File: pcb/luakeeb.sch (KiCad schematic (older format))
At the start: 121 parts, among them J1 Pimoroni, J2 Conn_01x04_Female, J3 Conn_01x04_Female, SW1 SW_Push, SW10 SW_Push, SW11 SW_Push, SW12 SW_Push, SW13 SW_Push, SW14 SW_Push, SW15 SW_Push, SW16 SW_Push, SW2 SW_Push, SW21 SW_Push, SW22 SW_Push, SW23 SW_Push, SW24 SW_Push, SW25 SW_Push, SW3 SW_Push, SW34 SW_Push, SW35 SW_Push, SW4 SW_Push, SW41 SW_Push, SW42 RotaryEncoder_Switch, SW5 SW_Push, SW6 SW_Push, SW7 RotaryEncoder_Switch, SW8 SW_Push, SW9 SW_Push, U1 ProMicro, U3 TRRS, U4 TRRS

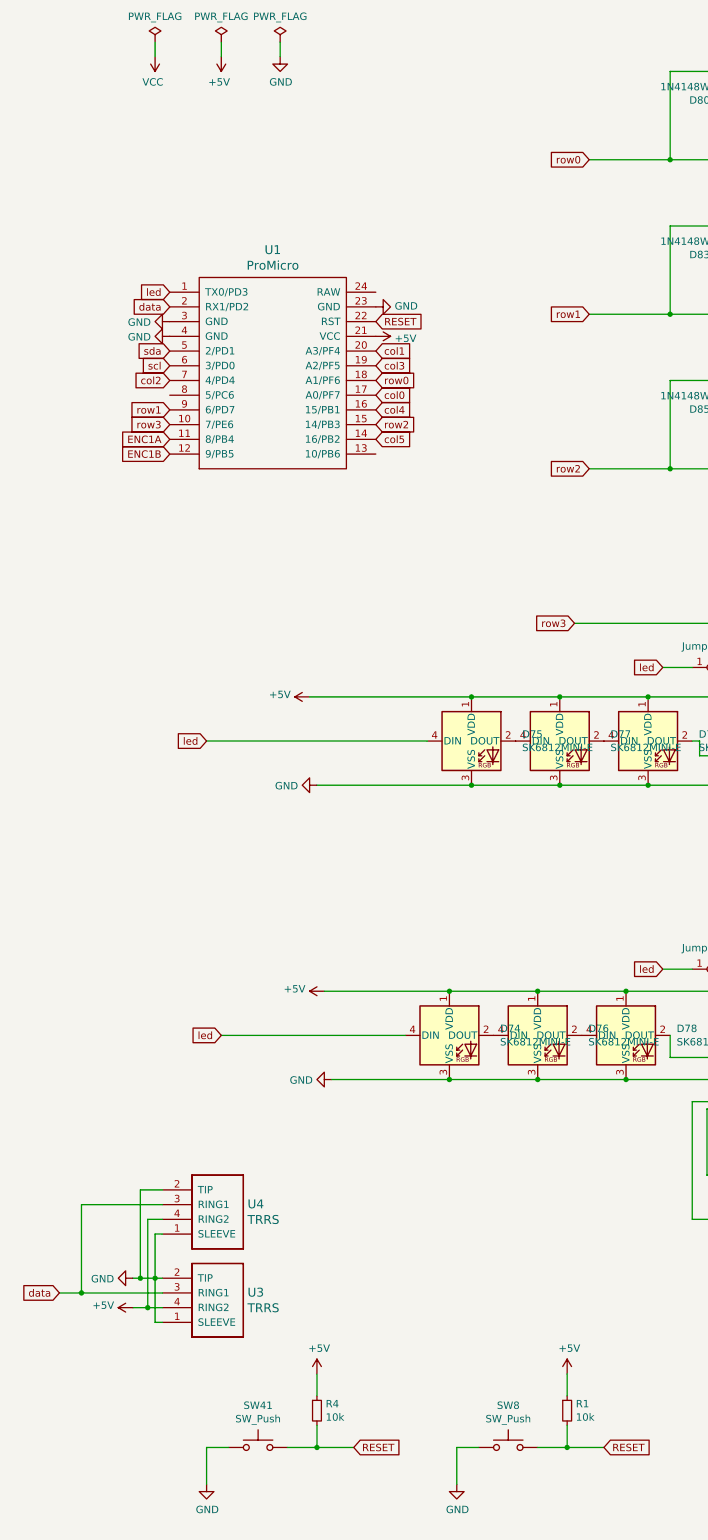
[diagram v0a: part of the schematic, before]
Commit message: added wireless support for nice nano with wiring, jst connector, and on off switch
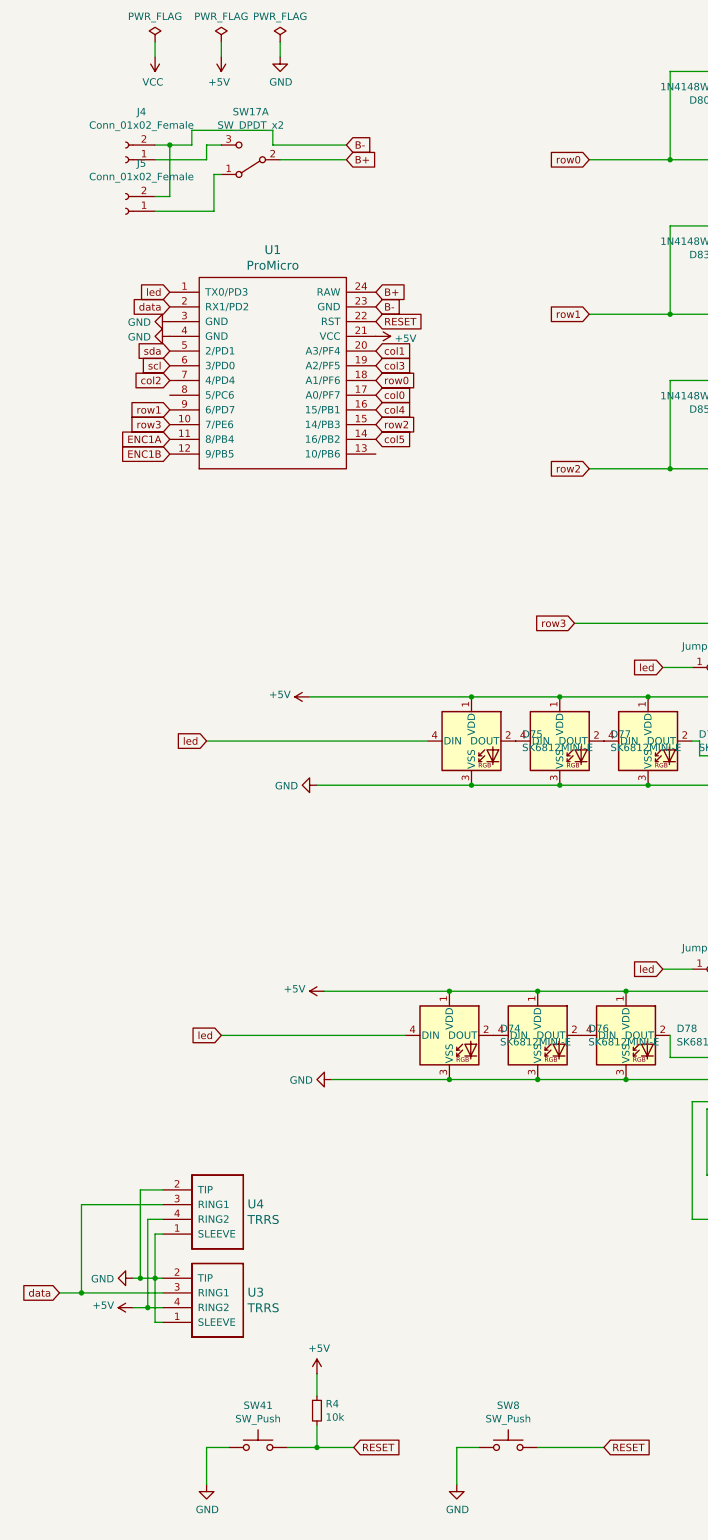
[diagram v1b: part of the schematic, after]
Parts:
- removed R1: 10k, Resistor_SMD:R_0805_2012Metric, symbol Device:R_Small
- added J4, J5: Conn_01x02_Female, Connector_JST:JST_PH_S2B-PH-K_1x02_P2.00mm_Horizontal, symbol Connector:Conn_01x02_Female
- added SW17: SW_DPDT_x2, Button_Switch_THT:SW_CuK_OS102011MA1QN1_SPDT_Angled, symbol Switch:SW_DPDT_x2
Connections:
- net GND: no longer U1.23 (GND)
- net B+: now reaches U1.24 (RAW)
- net B+: now also SW17.2 (B)
- new net: J4.1 (Pin_1), SW17.3 (C)
- new net: J5.1 (Pin_1), SW17.1 (A)
- new net B-: J4.2 (Pin_2), J5.2 (Pin_2), U1.23 (GND)
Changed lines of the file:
@@
 Text GLabel 1750 3450 0    50   Input ~ 0
 row1
-$Comp
-L power:GND #PWR0110
-U 1 1 613DF971
-P 3150 2750
-F 0 "#PWR0110" H 3150 2500 50  0001 C CNN
-F 1 "GND" V 3155 2622 50  0000 R CNN
-F 2 "" H 3150 2750 50  0001 C CNN
-F 3 "" H 3150 2750 50  0001 C CNN
-	1    3150 2750
-	0    -1   -1   0
-$EndComp
 Text GLabel 3150 3350 2    50   Input ~ 0
 col0
@@
 RESET
 $Comp
-L Device:R_Small R1
-U 1 1 61BC85AE
-P 4450 10250
-F 0 "R1" H 4509 10296 50  0000 L CNN
-F 1 "10k" H 4509 10205 50  0000 L CNN
-F 2 "Resistor_SMD:R_0805_2012Metric" H 4450 10250 50  0001 C CNN
-F 3 "~" H 4450 10250 50  0001 C CNN
-F 4 "C17414" H 4450 10250 50  0001 C CNN "LCSC"
-	1    4450 10250
-	1    0    0    -1
-$EndComp
-$Comp
-L power:+5V #PWR0116
-U 1 1 61BC85B4
-P 4450 10000
-F 0 "#PWR0116" H 4450 9850 50  0001 C CNN
-F 1 "+5V" H 4465 10173 50  0000 C CNN
-F 2 "" H 4450 10000 50  0001 C CNN
-F 3 "" H 4450 10000 50  0001 C CNN
-	1    4450 10000
-	1    0    0    -1
-$EndComp
-$Comp
 L power:GND #PWR0117
 U 1 1 61BC85BA
@@
 $EndComp
 Wire Wire Line
-	4700 10500 4450 10500
-Wire Wire Line
-	4450 10500 4450 10350
-Connection ~ 4450 10500
-Wire Wire Line
-	4450 10150 4450 10000
-Wire Wire Line
 	3700 10500 3700 10750
 $Comp
@@
 	1    0    0    -1
 $EndComp
-Wire Wire Line
-	4250 10500 4450 10500
 Wire Wire Line
 	3700 10500 3850 10500
@@
 Wire Wire Line
 	7650 9950 7750 9950
+$Comp
+L Connector:Conn_01x02_Female J4
+U 1 1 61BC80F1
+P 1450 1750
+F 0 "J4" H 1342 1425 50  0000 C CNN
+F 1 "Conn_01x02_Female" H 1342 1516 50  0000 C CNN
+F 2 "Connector_JST:JST_PH_S2B-PH-K_1x02_P2.00mm_Horizontal" H 1450 1750 50  0001 C CNN
+F 3 "~" H 1450 1750 50  0001 C CNN
+F 4 "C173752" H 1450 1750 50  0001 C CNN "LCSC"
+	1    1450 1750
+	-1   0    0    1
+$EndComp
+Text GLabel 3150 2750 2    50   Input ~ 0
+B-
+Text GLabel 3150 2650 2    50   Input ~ 0
+B+
+Text GLabel 2950 1750 2    50   Input ~ 0
+B+
+Text GLabel 2950 1650 2    50   Input ~ 0
+B-
+Wire Wire Line
+	1650 1650 1750 1650
+Wire Wire Line
+	1900 1650 1900 1550
+Wire Wire Line
+	1900 1550 2450 1550
+Wire Wire Line
+	2450 1550 2450 1650
+Wire Wire Line
+	2450 1650 2950 1650
+Wire Wire Line
+	2500 1750 2950 1750
+$Comp
+L Connector:Conn_01x02_Female J5
+U 1 1 61CE24AE
+P 1450 2100
+F 0 "J5" H 1342 1775 50  0000 C CNN
+F 1 "Conn_01x02_Female" H 1342 1866 50  0000 C CNN
+F 2 "Connector_JST:JST_PH_S2B-PH-K_1x02_P2.00mm_Horizontal" H 1450 2100 50  0001 C CNN
+F 3 "~" H 1450 2100 50  0001 C CNN
+F 4 "C173752" H 1450 2100 50  0001 C CNN "LCSC"
+	1    1450 2100
+	-1   0    0    1
+$EndComp
+Wire Wire Line
+	1650 2000 1750 2000
+Wire Wire Line
+	1750 2000 1750 1650
+Connection ~ 1750 1650
+Wire Wire Line
+	1750 1650 1900 1650
+$Comp
+L Switch:SW_DPDT_x2 SW17
+U 1 1 61E32BEB
+P 2300 1750
+F 0 "SW17" H 2300 1425 50  0000 C CNN
+F 1 "SW_DPDT_x2" H 2300 1516 50  0000 C CNN
+F 2 "Button_Switch_THT:SW_CuK_OS102011MA1QN1_SPDT_Angled" H 2300 1750 50  0001 C CNN
+F 3 "~" H 2300 1750 50  0001 C CNN
+F 4 "C226259" H 2300 1750 50  0001 C CNN "LCSC"
+	1    2300 1750
+	-1   0    0    1
+$EndComp
+Wire Wire Line
+	2000 1750 2000 1650
+Wire Wire Line
+	2000 1650 2100 1650
+Wire Wire Line
+	1650 1750 2000 1750
+Wire Wire Line
+	2050 2100 2050 1850
+Wire Wire Line
+	2050 1850 2100 1850
+Wire Wire Line
+	1650 2100 2050 2100
+Wire Wire Line
+	4250 10500 4700 10500
 $EndSCHEMATC
